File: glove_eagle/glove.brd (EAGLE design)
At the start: 63.5 x 38.1 mm, 51 parts, among them J1 MICRO_USB_B_JST_MC5BR3-M404-4S, U1 BNO055, U3 NRF51822QF, U4 MCP73831, X3 ABS05-32.768KHZ-9-T

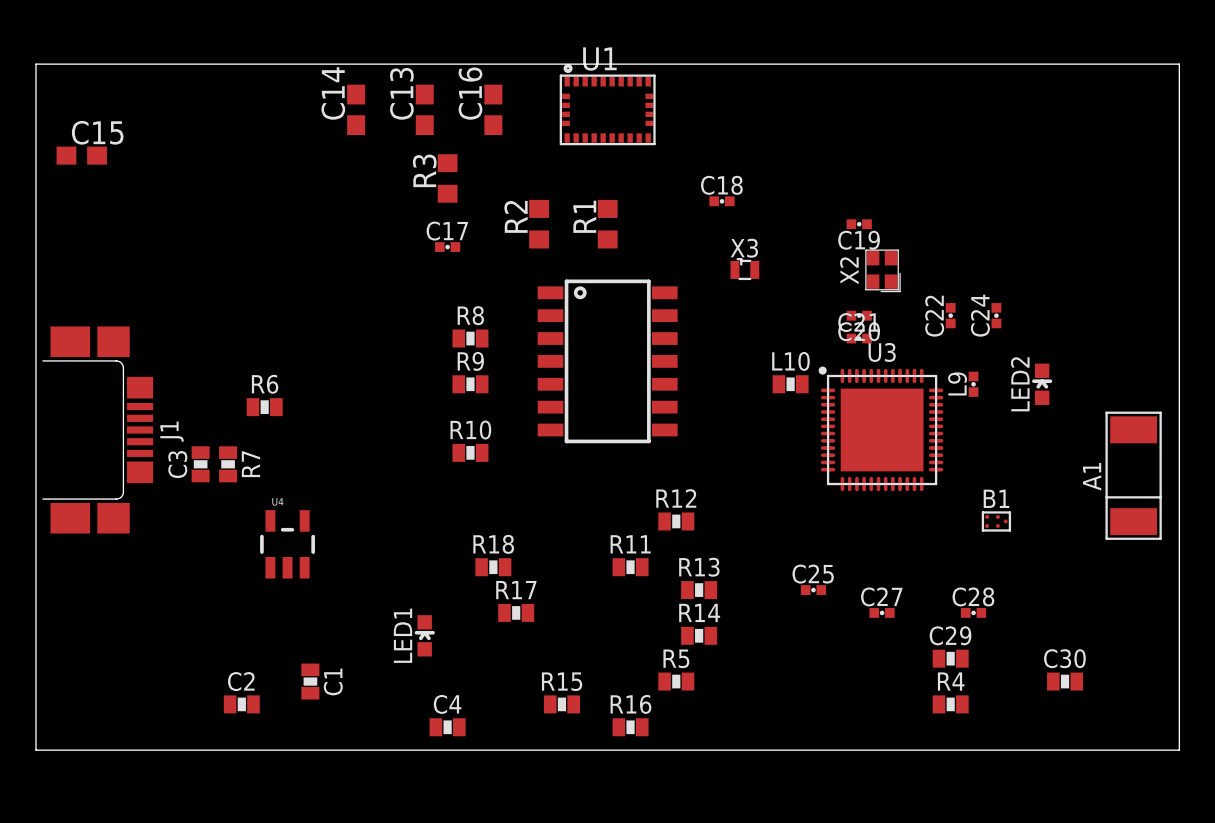
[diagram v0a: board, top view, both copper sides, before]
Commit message: Finished routing nearly complete board
Still lots of modifications to make, but it's a start.
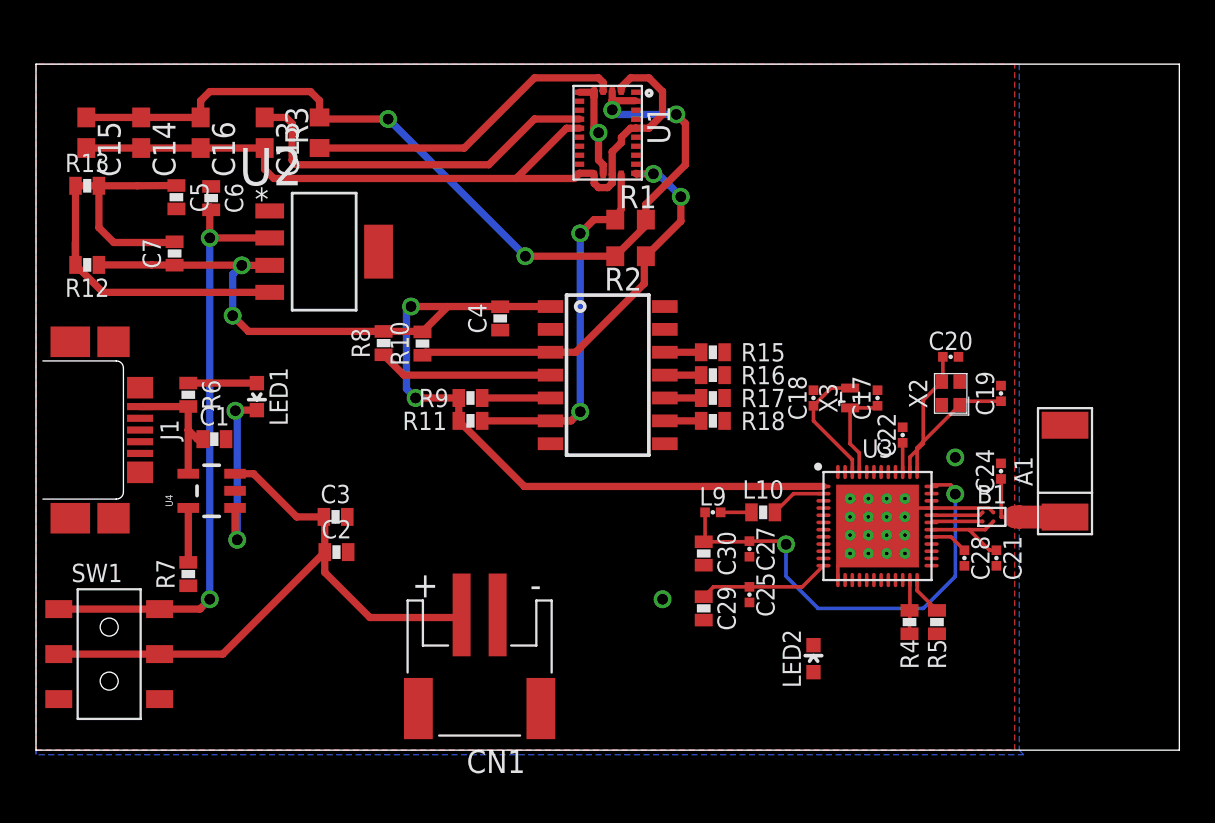
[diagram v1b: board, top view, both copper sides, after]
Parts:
- removed R14: (no value), passives:0603-RES
- added C5: (no value), passives:0603_CAP
- added C6, C7: 10 uF, passives:0603_CAP
- added CN1: (no value), adafruit:JST-PH-2-SMT-RA
- added SW1: (no value), adafruit:EG1390
- added U2: LP3855EMP-ADJ, LP3855EMP-ADJ:SOT150P696X180-5N
- R15, R16, R17, R18: value (none) -> 10 k
- R9: value (none) -> 47 k
- moved R13 40.7 mm to (2.84, 31.3)
- moved R12 35.7 mm to (2.84, 26.9), turned to 180 degrees
- moved C17 25.3 mm to (46.7, 19.6), turned to 90 degrees
- moved C4 22.9 mm to (25.8, 24.0), turned to 270 degrees
- moved C30 21.3 mm to (37.1, 10.9), turned to 270 degrees
- moved R15 21.3 mm to (37.6, 22.1), turned to 180 degrees
- moved R16 20.1 mm to (37.6, 20.8), turned to 180 degrees
- moved LED2 19.8 mm to (43.2, 5.08)
- moved C16 16.3 mm to (9.14, 34.3), turned to 270 degrees
- moved LED1 16.2 mm to (12.3, 19.6), turned to 180 degrees
- moved R17 16.2 mm to (37.6, 19.6), turned to 180 degrees
- moved L9 16.1 mm to (37.6, 13.2), turned to 0 degrees
- moved R5 14.8 mm to (50.0, 7.11), turned to 90 degrees
- moved R18 14.7 mm to (37.6, 18.3), turned to 180 degrees
- moved C1 14.5 mm to (9.91, 17.3), turned to 0 degrees
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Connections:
- removed net I2C_ADDR_SEL: U1.17
- removed net N$10: R13.1
- removed net N$11: R14.2, U$1.P$9
- removed net N$13: R14.1
- removed net N$6: R12.2, U$1.P$7
- removed net N$8: R13.2, U$1.P$8
- new net N$5: C6.2, SW1.O1, SW1.O2, U2.2
- net GND: now also C6.1, C7.2, CN1.2, R13.2, U1.17, U2.5
- net N$1: now also CN1.1, SW1.P1, SW1.P2
- net N$7: now also C5.1, R12.2, R13.1, U2.4; no longer R12.1
- net VCC: now also C7.1, R12.1, U2.3
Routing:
- net VCC: track 0.00 -> 71.4 mm, vias 0 -> 4
- net VDD: track 0.00 -> 50.6 mm, vias 0 -> 4
- net GNDIO: track 0.00 -> 46.0 mm
- net GND: track 0.00 -> 38.9 mm, vias 0 -> 19
- net N$1: track 0.00 -> 34.8 mm
- net N$5: track 0.00 -> 33.9 mm, vias 0 -> 2
- net N$16: track 0.00 -> 25.7 mm, vias 0 -> 2
- net SDA: track 0.00 -> 22.7 mm, vias 0 -> 2
- net N$7: track 0.00 -> 22.7 mm
- net N$9: track 0.00 -> 20.8 mm
- net SCL: track 0.00 -> 20.7 mm, vias 0 -> 2
- net N$18: track 0.00 -> 18.0 mm
- net N$3: track 0.00 -> 10.4 mm, vias 0 -> 2
- net N$40: track 0.00 -> 9.74 mm
- net N$38: track 0.00 -> 7.44 mm
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- added copper zone on layer 1, net GND
- added copper zone on layer 16, net GND

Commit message: Added traces to board for I2C
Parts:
- added J2: TC2030-JLINK-NL, connector:TC2030-IDC-NL
- added R14: 1k, passives:0603-RES
- C5: value (none) -> 8 nF
- R12: value (none) -> 440
- R13: value (none) -> 250
- moved L9 2.29 mm to (35.3, 13.2)
- moved C30 2.03 mm to (35.1, 10.9)
- moved LED2 1.48 mm to (44.5, 5.84)
- moved L10 1.27 mm to (39.1, 13.2)
- moved C27 0.76 mm to (38.9, 11.2)
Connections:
- new net FLEX0: U3.5
- new net FLEX1: U3.6
- new net FLEX2: U3.7
- new net FLEX3: U3.8
- new net N$6: LED2.C, U3.19
- new net N$8: LED2.A, R14.1
- new net SLCK: U3.15
- net GND: now also J2.5
- net N$19: now also J2.2
- net N$30: now also J2.4
- net SCL: now also U3.11
- net SDA: now also U3.14
- net VCC: now also C5.2, J2.1, R14.2
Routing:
- net SDA: track 22.7 -> 51.8 mm, vias 2 -> 4
- net N$30: track 2.14 -> 26.0 mm
- net SCL: track 20.7 -> 40.5 mm, vias 2 -> 3
- net N$19: track 2.98 -> 17.0 mm
- net VCC: track 71.4 -> 82.4 mm
- net N$6: track 0.00 -> 3.88 mm
- net N$16: track 25.7 -> 29.2 mm
- net N$8: track 0.00 -> 3.30 mm
- net N$14: track 3.13 -> 4.40 mm
- net N$15: track 1.71 -> 2.73 mm
- net GND: track 38.9 -> 38.0 mm, vias 19 -> 22
